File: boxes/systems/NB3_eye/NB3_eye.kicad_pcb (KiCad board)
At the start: 2 copper layers, 51 x 16 mm, 2 parts, among them J1 2x5_Pin_Header_side, J3 Socket_1x5_side

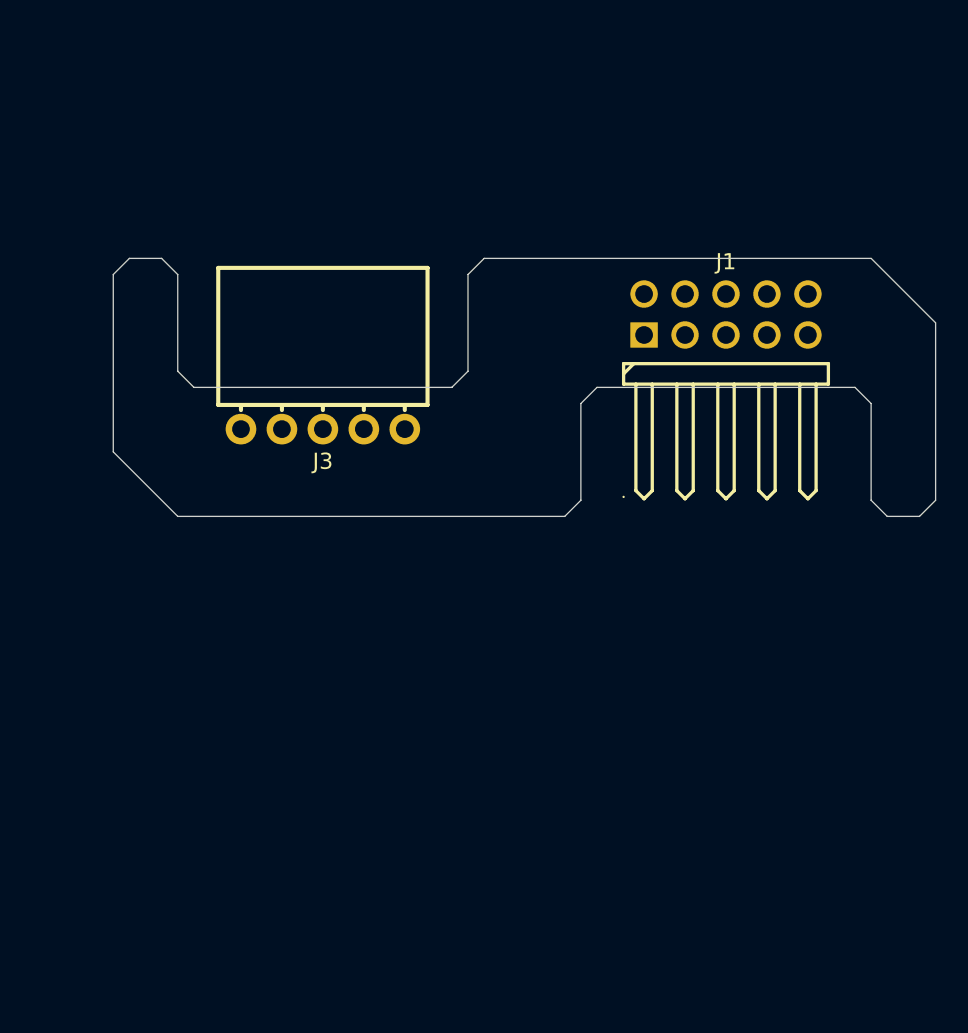
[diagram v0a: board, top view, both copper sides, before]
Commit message: Update fabrication details for NB3 eye
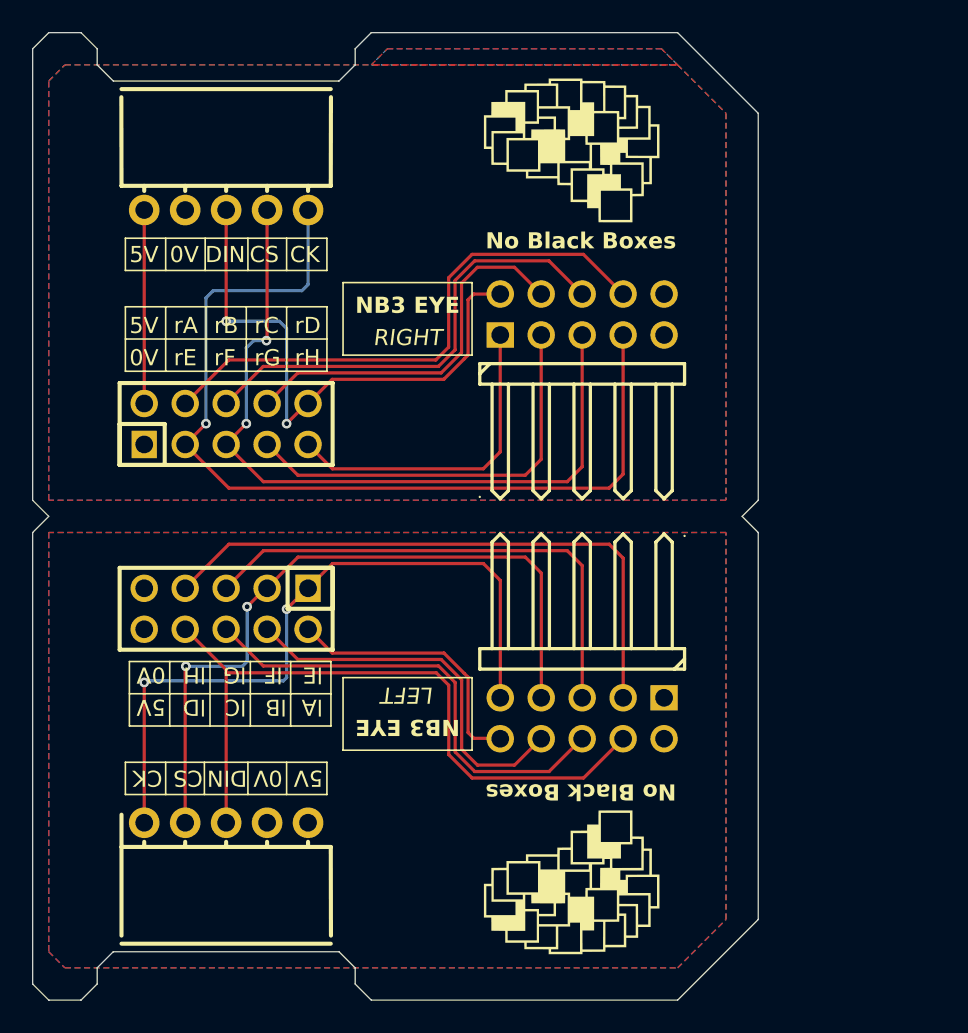
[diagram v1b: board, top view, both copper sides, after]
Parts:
- added G***: LOGO, NB3_eye:Logo_NBB_15mm, F.Cu at (124.5, 86.0)
- added G***: LOGO, NB3_eye:Logo_VK_5mm, B.Cu at (127.0, 127.0)
- added G***: LOGO, NB3_eye:Logo_NBB_15mm, B.Cu at (124.5, 132.0)
- added G***: LOGO, NB3_eye:Logo_VK_5mm, B.Cu at (127.0, 91.0)
- added J2: 2x5_Pin_Header_side, NB3_eye:PinHeader_Male_TH_Side_2x5_C60563, F.Cu at (125.1, 121.5)
- added J4: Socket_1x5_side, NB3_eye:SocketHeader_Female_TH_Side_1x5_C2897387, F.Cu at (103.0, 128.0)
- added J5: 2x5_Socket_Vertical, NB3_eye:SocketHeader_Female_TH_2x5_C492399, F.Cu at (103.0, 103.3)
- added J6: 2x5_Socket_Vertical, NB3_eye:SocketHeader_Female_TH_2x5_C492399, F.Cu at (103.0, 114.7)
- moved J3 14.9 mm to (103.0, 90.0)
- moved J1 8.92 mm to (125.1, 96.5)
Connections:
- J1 pad 1: unconnected-(J1-Pad1) -> /rH
- J1 pad 10: unconnected-(J1-Pad10) -> +5V
- J1 pad 2: unconnected-(J1-Pad2) -> /rD
- J1 pad 3: unconnected-(J1-Pad3) -> /rG
- J1 pad 4: unconnected-(J1-Pad4) -> /rC
- J1 pad 5: unconnected-(J1-Pad5) -> /rF
- J1 pad 6: unconnected-(J1-Pad6) -> /rB
- J1 pad 7: unconnected-(J1-Pad7) -> /rE
- J1 pad 8: unconnected-(J1-Pad8) -> /rA
- J1 pad 9: unconnected-(J1-Pad9) -> GND
- J3 pad 1: unconnected-(J3-Pad1) -> /rE
- J3 pad 2: unconnected-(J3-Pad2) -> /rF
- J3 pad 3: unconnected-(J3-Pad3) -> /rD
- J3 pad 4: unconnected-(J3-Pad4) -> GND
- J3 pad 5: unconnected-(J3-Pad5) -> +5V
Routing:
- net /rE: track 0.00 -> 58.2 mm, vias 0 -> 1
- net /rF: track 0.00 -> 47.7 mm, vias 0 -> 2
- net /lF: track 0.00 -> 44.7 mm, vias 0 -> 2
- net /lE: track 0.00 -> 44.0 mm, vias 0 -> 2
- net /lD: track 0.00 -> 43.9 mm
- net /lH: track 0.00 -> 37.3 mm
- net /rD: track 0.00 -> 35.2 mm, vias 0 -> 2
- net /rA: track 0.00 -> 34.5 mm
- net /lG: track 0.00 -> 31.6 mm
- net /lC: track 0.00 -> 29.1 mm
- net /rB: track 0.00 -> 29.1 mm
- net /rG: track 0.00 -> 25.9 mm
- net /rC: track 0.00 -> 23.7 mm
- net /lB: track 0.00 -> 23.7 mm
- net /rH: track 0.00 -> 20.2 mm
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- added copper zone on F.Cu, net +5V
- added copper zone on B.Cu, net GND
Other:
- board size 51 x 16 mm -> 45 x 60 mm
- board text added: "0V"
- board text added: "5V"
- board text added: "CK"
- board text added: "CS"
- board text added: "DIN"
- board text added: "For Research and Education ONLY"
- board text added: "LEFT"
- board text added: "NB3 EYE"
- board text added: "No Black Boxes"
- board text added: "RIGHT"
- board text added: "Rev 0.0.1"
- board text added: "lA"
- board text added: "lB"
- board text added: "lC"
- board text added: "lD"
- board text added: "lE"
- board text added: "lF"
- board text added: "lG"
- board text added: "lH"
- board text added: "rA"
- board text added: "rB"
- board text added: "rC"
- board text added: "rD"
- board text added: "rE"
- board text added: "rF"
- board text added: "rG"
- board text added: "rH"
